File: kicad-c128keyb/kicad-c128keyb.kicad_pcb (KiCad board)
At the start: 2 copper layers, 67.3 x 58.1 mm, 19 parts, among them J1 KBD_FLAT26, J2 DB25_Male_MountingHoles, J3 OLED_128x32, J4 EXT_POWER_5V, Q1 2N3904, Q2 2N3904, Q3 2N3904, U1 MT8816, U2 74HC595, U3 SeeeduinoXIAO

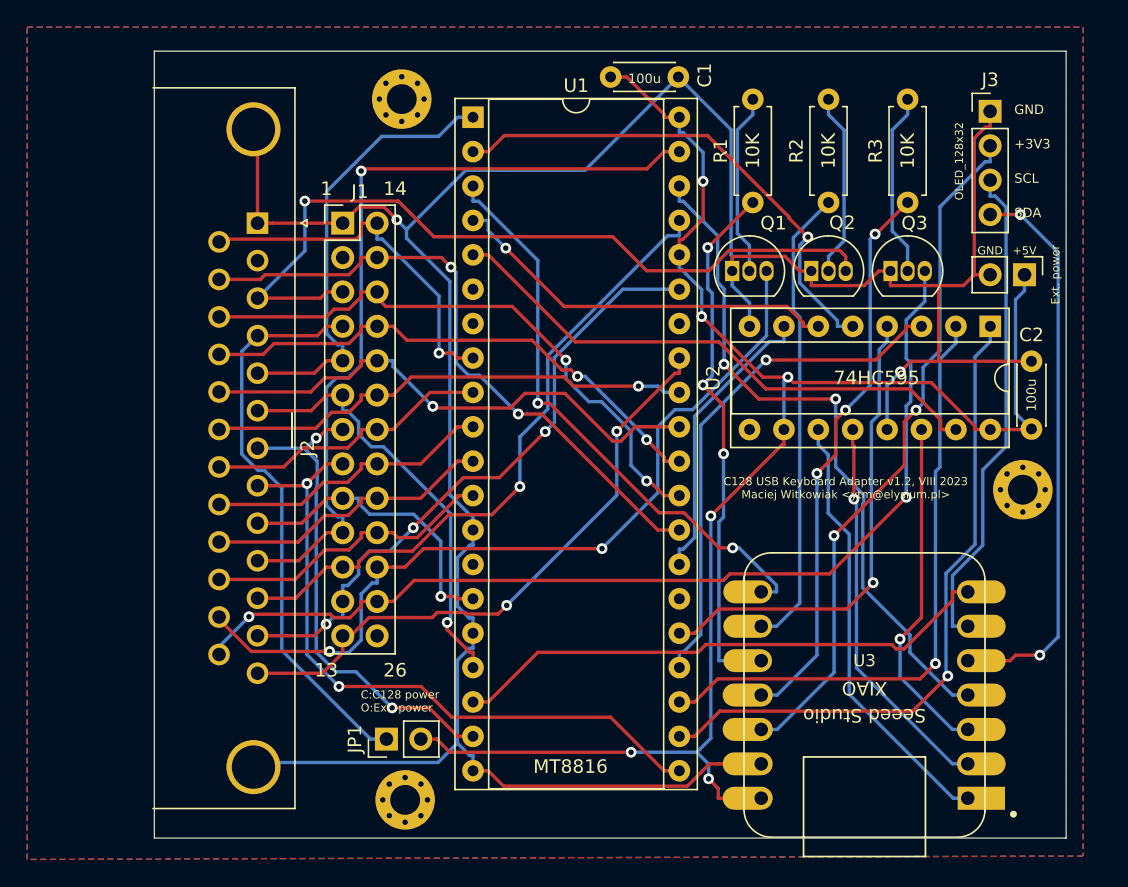
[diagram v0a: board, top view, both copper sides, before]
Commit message: common C16/C64 version for internal mount; despite filenames this is not about C128 anymore; downgraded from MT8816 to MT8808
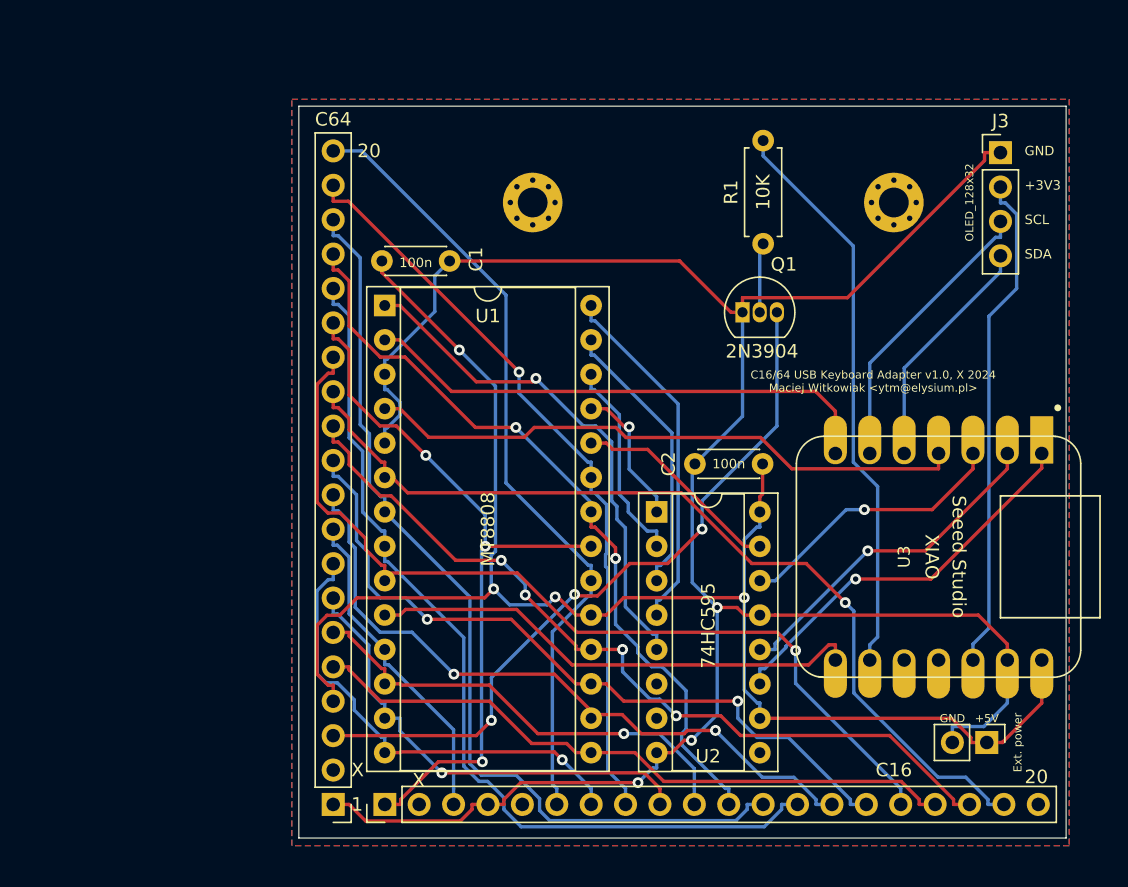
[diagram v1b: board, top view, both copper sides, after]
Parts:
- removed J1: KBD_FLAT26, Connector_PinHeader_2.54mm:PinHeader_2x13_P2.54mm_Vertical
- removed JP1: EXT_POWER_EN, Connector_PinHeader_2.54mm:PinHeader_1x02_P2.54mm_Vertical
- removed Q2, Q3: 2N3904, Package_TO_SOT_THT:TO-92_Inline
- removed R2, R3: 10K, Resistor_THT:R_Axial_DIN0207_L6.3mm_D2.5mm_P7.62mm_Horizontal
- removed REF3: MountingHole, MountingHole:MountingHole_2.2mm_M2_Pad_Via
- added J5: C16, Connector_PinHeader_2.54mm:PinHeader_1x20_P2.54mm_Vertical, F.Cu at (111.0, 116.6)
- C1, C2: value 100u -> 100n
- J2: value DB25_Male_MountingHoles -> C64; footprint Connector_Dsub:DSUB-25_Male_Horizontal_P2.77x2.84mm_EdgePinOffset4.94mm_Housed_MountingHolesOffset7.48mm -> Connector_PinHeader_2.54mm:PinHeader_1x20_P2.54mm_Vertical
- U1: value MT8816 -> MT8808; footprint Package_DIP:DIP-40_W15.24mm_Socket -> Package_DIP:DIP-28_W15.24mm_Socket
- moved REF2 45.1 mm to (121.9, 72.1)
- moved J2 43.3 mm to (107.2, 116.6), turned to 180 degrees
- moved REF1 37.1 mm to (148.6, 72.1)
- moved J4 34.7 mm to (155.5, 112.0)
- moved U2 28.2 mm to (131.1, 95.0), turned to 0 degrees
- moved C1 21.7 mm to (110.8, 76.5)
- moved C2 20.0 mm to (138.9, 91.4), turned to 180 degrees
- moved U1 15.4 mm to (111.0, 79.7)
- moved U3 11.6 mm to (151.9, 98.3), turned to -90 degrees
- moved J3 3.14 mm to (156.5, 68.5)
- moved Q1 3.14 mm to (137.4, 80.2)
- moved R1 3.14 mm to (138.9, 75.2)
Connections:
- J2 pad 4: Net-(J1-Pad4) -> VCC
- Q1 pad 3: /40/80 -> /~{RESTORE}
- R1 pad 1: /40/80_3V -> Net-(Q1-Pad2)
- R1 pad 2: Net-(Q1-Pad2) -> /~{RESTORE_3V}
- U1 pad 1: /PB3 -> /AY2
- U1 pad 10: /K0 -> /RESET
- U1 pad 11: /K1 -> /PB7
- U1 pad 12: /K2 -> /PB6
- U1 pad 13: GND -> /PB5
- U1 pad 14: unconnected-(U1-Pad14) -> /PB4
- U1 pad 15: /PB7 -> /PB3
- U1 pad 16: GND -> /PB2
- U1 pad 17: /PB6 -> /PB1
- U1 pad 18: /STROBE -> /PB0
- U1 pad 19: /PB5 -> VCC
- U1 pad 2: Net-(U1-Pad2) -> /STROBE
- U1 pad 20: GND -> /PA7
- U1 pad 21: /PB4 -> /PA5
- U1 pad 22: Net-(U1-Pad22) -> /PA3
- U1 pad 23: Net-(U1-Pad23) -> /PA1
- U1 pad 24: Net-(U1-Pad24) -> /AX0
- U1 pad 25: Net-(U1-Pad25) -> /AX1
- U1 pad 26: unconnected-(U1-Pad26) -> /AX2
- U1 pad 27: /UNUSED -> /AY0
- U1 pad 28: /PA5 -> /AY1
- U1 pad 3: /RESET -> GND
- U1 pad 4: Net-(U1-Pad4) -> /DATA
- U1 pad 5: Net-(U1-Pad5) -> GND
- U1 pad 6: unconnected-(U1-Pad6) -> /PA0
- U1 pad 7: unconnected-(U1-Pad7) -> /PA2
- U1 pad 8: /PA6 -> /PA4
- U1 pad 9: /PA7 -> /PA6
- U2 pad 1: Net-(U1-Pad22) -> /AX1
- U2 pad 15: Net-(U1-Pad5) -> /AX0
- U2 pad 2: Net-(U1-Pad23) -> /AX2
- U2 pad 3: Net-(U1-Pad24) -> /AY0
- U2 pad 4: Net-(U1-Pad25) -> /AY1
- U2 pad 5: Net-(U1-Pad2) -> /AY2
- U2 pad 6: Net-(U1-Pad4) -> unconnected-(U2-Pad6)
- U2 pad 7: /UNUSED -> unconnected-(U2-Pad7)
- U3 pad 10: /40/80_3V -> unconnected-(U3-Pad10)
- U3 pad 11: /CAPS_3V -> unconnected-(U3-Pad11)
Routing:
- net /CAPS: track 73.9 -> 0.00 mm, vias 2 -> 0
- net /40/80: track 61.6 -> 0.00 mm, vias 2 -> 0
- net Net-(U1-Pad22): track 48.9 -> 0.00 mm, vias 1 -> 0
- net Net-(U1-Pad23): track 45.6 -> 0.00 mm, vias 1 -> 0
- net Net-(J1-Pad4): track 42.2 -> 0.00 mm
- net /CAPS_3V: track 41.6 -> 0.00 mm, vias 3 -> 0
- net Net-(U1-Pad5): track 41.4 -> 0.00 mm
- net GND: track 204.0 -> 162.9 mm, vias 2 -> 3
- net /PA6: track 27.1 -> 67.2 mm
- net /40/80_3V: track 39.5 -> 0.00 mm, vias 3 -> 0
- net Net-(U1-Pad24): track 38.2 -> 0.00 mm, vias 1 -> 0
- net /AY2: track 0.00 -> 38.0 mm, vias 0 -> 1
- net /PA7: track 21.2 -> 58.9 mm
- net Net-(U1-Pad2): track 37.5 -> 0.00 mm, vias 1 -> 0
- net Net-(U1-Pad25): track 35.3 -> 0.00 mm, vias 1 -> 0
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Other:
- board size 67.3 x 58.1 mm -> 56.7 x 54 mm
- board text added: "20"
- board text added: "C16/64 USB Keyboard Adapter v1.0, X 2024 Maciej Witkowiak <ytm@elysium.pl>"
- board text added: "X"
- board text removed: "13"
- board text removed: "14"
- board text removed: "26"
- board text removed: "C128 USB Keyboard Adapter v1.2, VIII 2023 Maciej Witkowiak <ytm@elysium.pl>"
- board text removed: "C:C128 power O:Ext. power"
